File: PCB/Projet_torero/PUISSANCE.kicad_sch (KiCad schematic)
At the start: 0 parts

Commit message: add kicad puissance
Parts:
- added C301, C302, C303, C304: C_Small, symbol Device:C_Small
- added J301, J302: Conn_01x02, symbol Connector_Generic:Conn_01x02
- added R301, R302, R303, R304: R_Small, symbol Device:R_Small
- added U301, U302: ZXBM5210-SP, Package_SO:Diodes_SO-8EP, symbol Driver_Motor:ZXBM5210-SP
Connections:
- new net: J302.1 (Pin_1), U302.1 (OUT1)
- new net: R303.2, R304.1, U302.6 (VREF)
- new net: J302.2 (Pin_2), U302.7 (OUT2)
- new net: J301.1 (Pin_1), U301.1 (OUT1)
- new net: J301.2 (Pin_2), U301.7 (OUT2)
- new net: R301.2, R302.1, U301.6 (VREF)
- new net +3.3V: C301.2, C303.2, R301.1, R303.1, U301.3 (VDD), U302.3 (VDD)
- new net FWDD: U302.4 (FWD)
- new net FWDG: U301.4 (FWD)
- new net GND: C301.1, C302.2, C303.1, C304.2, R302.2, R304.2, U301.8 (GND), U301.9 (GND), U302.8 (GND), U302.9 (GND)
- new net REVD: U302.5 (REV)
- new net REVG: U301.5 (REV)
- new net V7.2: C302.1, C304.1, U301.2 (VM), U302.2 (VM)
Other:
- note added: "MOTEUR DROIT"
- note added: "MOTEUR GAUCHE"

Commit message: Add files via upload
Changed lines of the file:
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@@
-		)
-	)
-	(hierarchical_label "V7.2"
-		(shape input)
-		(at 25.4 116.84 180)
-		(fields_autoplaced yes)
-		(effects
-			(font
-				(size 1.27 1.27)
-			)
-			(justify right)
 		)
 	)
@@
 		(fields_autoplaced yes)
 		(effects
-			(font
-				(size 1.27 1.27)
-			)
-			(justify right)
-		)
-	)
-	(hierarchical_label "V7.2"
-		(shape input)
-		(at 133.35 116.84 180)
-		(fields_autoplaced yes)
-		(effects

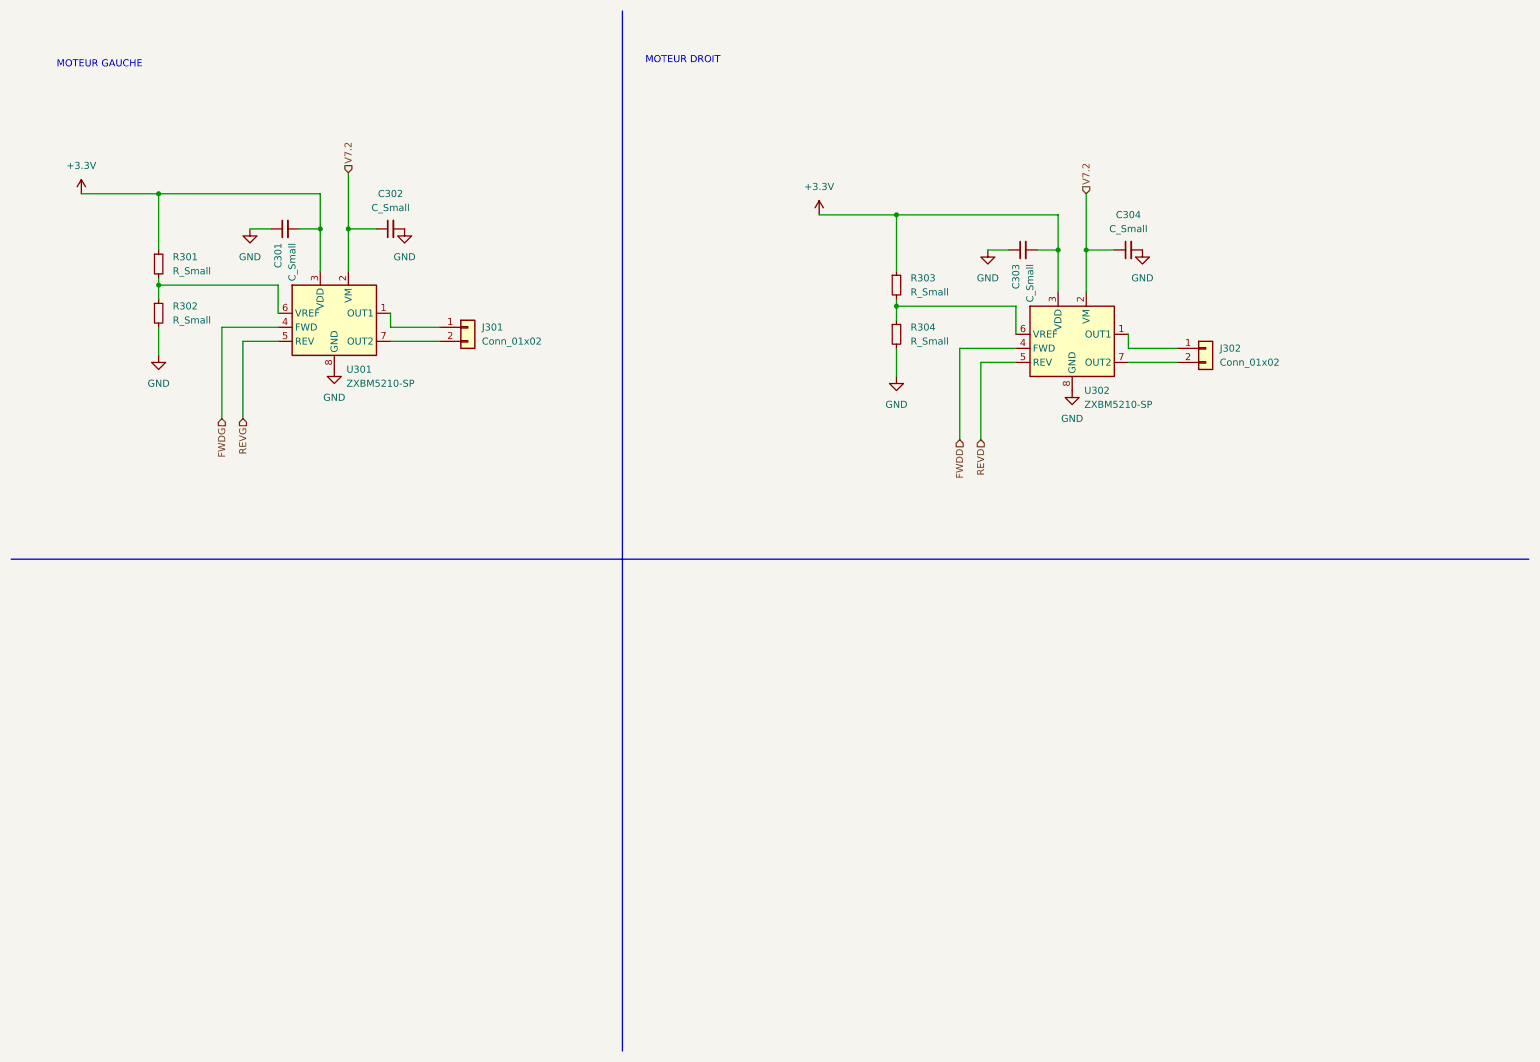
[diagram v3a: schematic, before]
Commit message: modification moteurs et alim
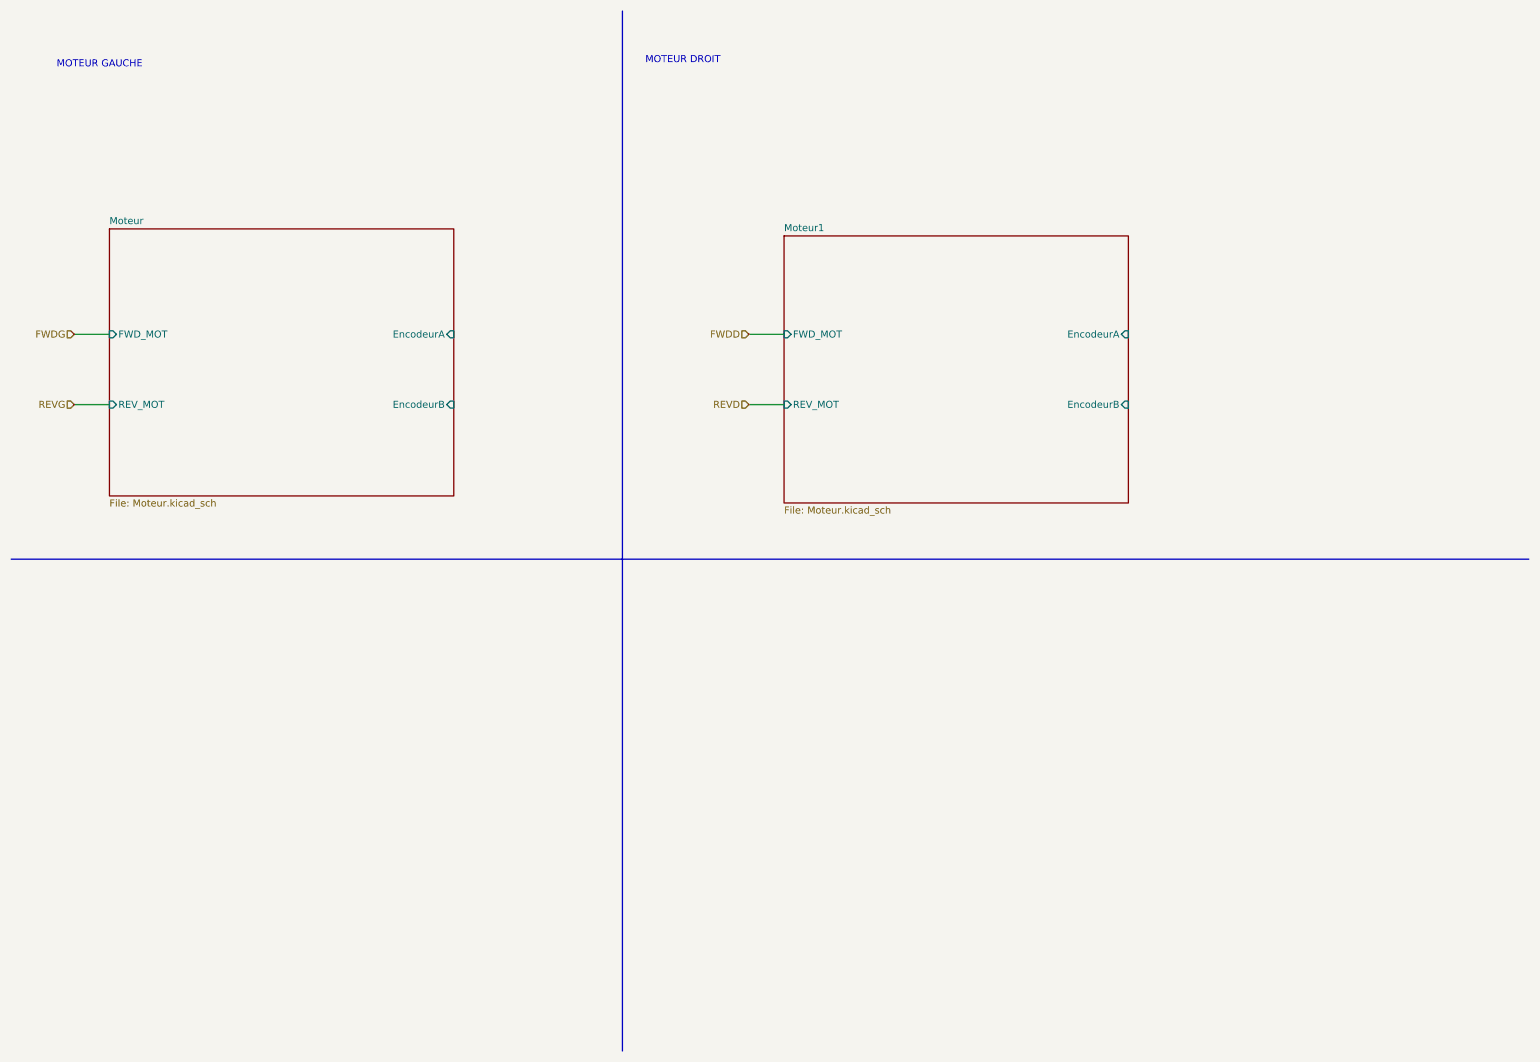
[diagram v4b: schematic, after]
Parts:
- removed C301, C302, C303, C304: C_Small, symbol Device:C_Small
- removed J301, J302: Conn_01x02, symbol Connector_Generic:Conn_01x02
- removed R301, R302, R303, R304: R_Small, symbol Device:R_Small
- removed U301, U302: ZXBM5210-SP, Package_SO:Diodes_SO-8EP, symbol Driver_Motor:ZXBM5210-SP
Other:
- added sheet Moteur (Moteur.kicad_sch)
- added sheet Moteur1 (Moteur.kicad_sch)

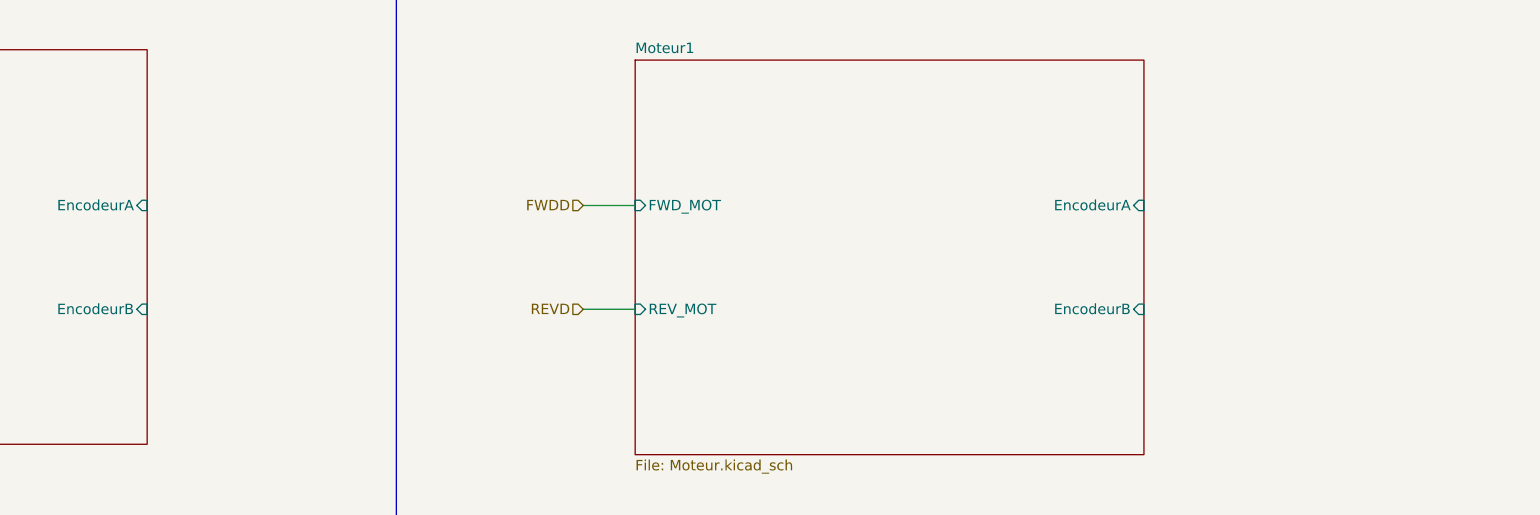
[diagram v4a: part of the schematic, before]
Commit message: Mit à jour les encodeurs
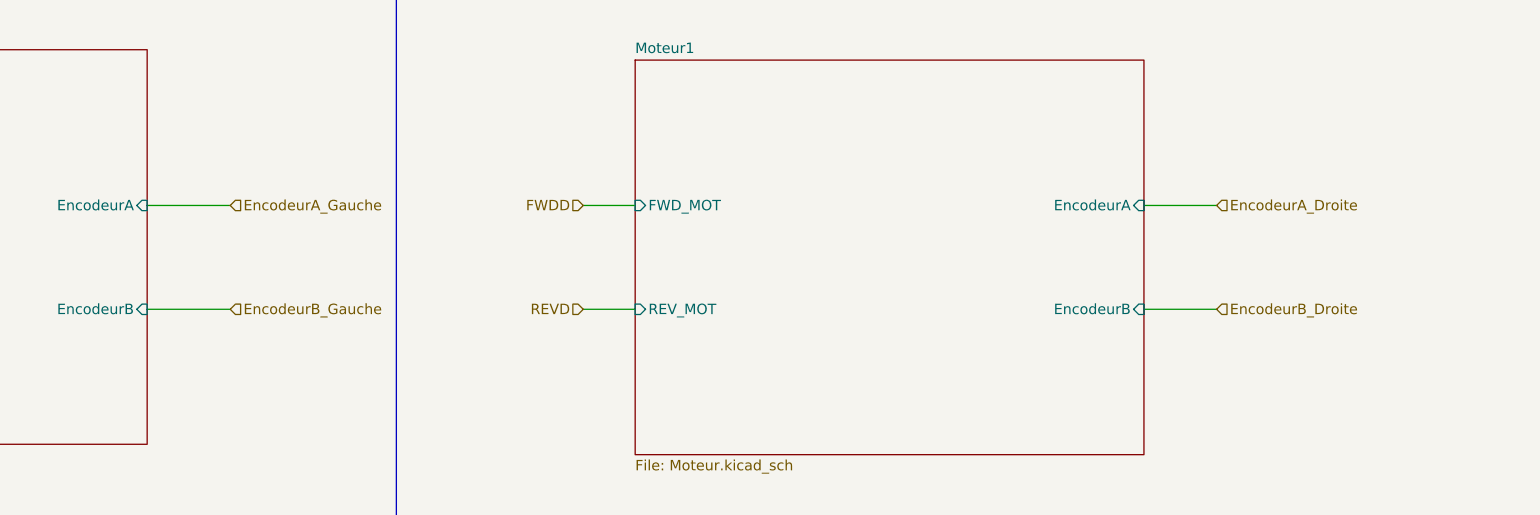
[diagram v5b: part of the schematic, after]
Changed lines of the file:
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@@
+	(wire
+		(pts
+			(xy 92.71 82.55) (xy 102.87 82.55)
+		)
+		(stroke
+			(width 0)
+			(type default)
+		)
+	)
+	(wire
+		(pts
+			(xy 214.63 69.85) (xy 223.52 69.85)
+		)
+		(stroke
+			(width 0)
+			(type default)
+		)
+	)
 	(wire
 		(pts
@@
 		(pts
 			(xy 123.19 110.49) (xy 123.19 199.39)
+		)
+		(stroke
+			(width 0)
+			(type default)
+		)
+	)
+	(wire
+		(pts
+			(xy 92.71 69.85) (xy 102.87 69.85)
+		)
+		(stroke
+			(width 0)
+			(type default)
+		)
+	)
+	(wire
+		(pts
+			(xy 214.63 82.55) (xy 223.52 82.55)
 		)
 		(stroke
@@
 				(size 1.27 1.27)
 			)
+		)
+	)
+	(hierarchical_label "EncodeurA_Droite"
+		(shape input)
+		(at 223.52 69.85 0)
+		(fields_autoplaced yes)
+		(effects
+			(font
+				(size 1.27 1.27)
+			)
+			(justify left)
 		)
 	)
@@
 		)
 	)
+	(hierarchical_label "EncodeurB_Gauche"
+		(shape input)
+		(at 102.87 82.55 0)
+		(fields_autoplaced yes)
+		(effects
+			(font
+				(size 1.27 1.27)
+			)
+			(justify left)
+		)
+	)
 	(hierarchical_label "REVG"
 		(shape input)
@@
 		)
 	)
+	(hierarchical_label "EncodeurB_Droite"
+		(shape input)
+		(at 223.52 82.55 0)
+		(fields_autoplaced yes)
+		(effects
+			(font
+				(size 1.27 1.27)
+			)
+			(justify left)
+		)
+	)
+	(hierarchical_label "EncodeurA_Gauche"
+		(shape input)
+		(at 102.87 69.85 0)
+		(fields_autoplaced yes)
+		(effects
+			(font
+				(size 1.27 1.27)
+			)
+			(justify left)
+		)
+	)
